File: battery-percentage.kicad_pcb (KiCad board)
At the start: 2 copper layers, 52.1 x 40.6 mm, 11 parts, among them J1 Conn_01x04_Pin, SW1 SW_Push, U1 WeMos_D1_mini, U2 LM7805_TO220

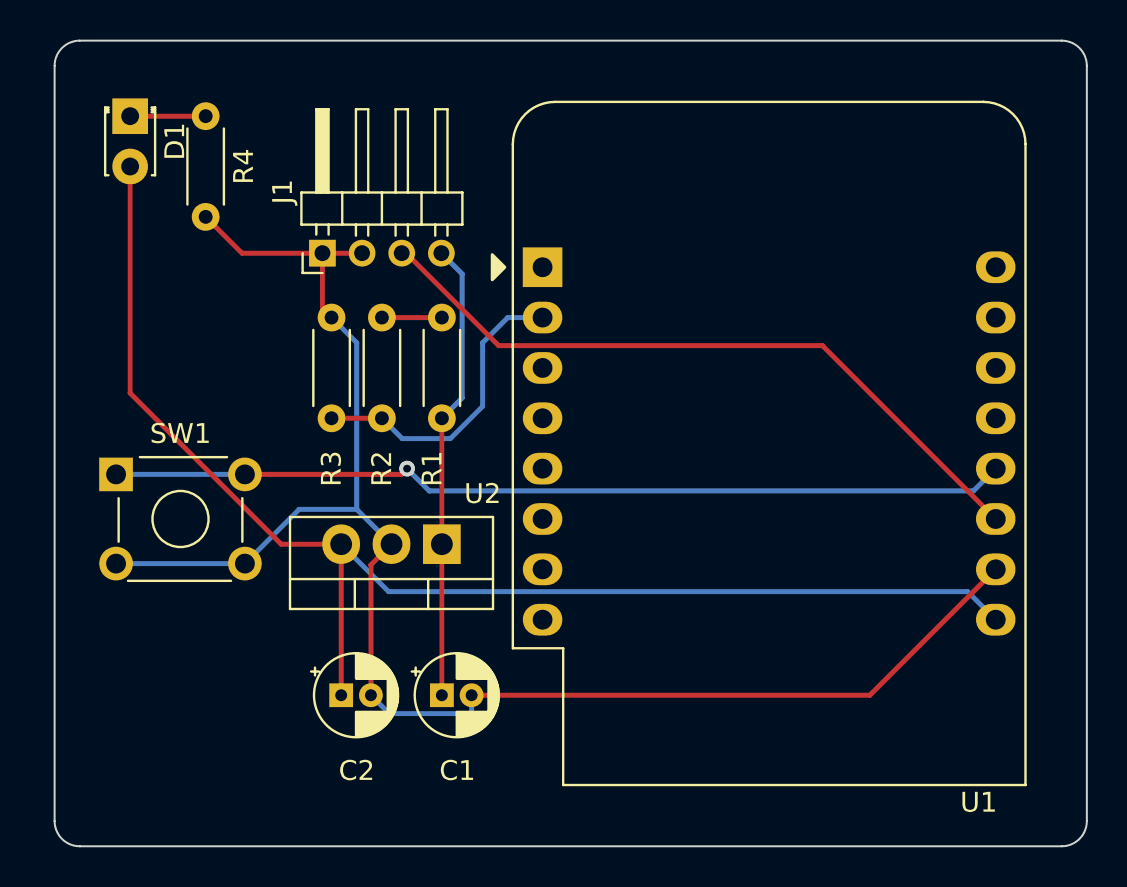
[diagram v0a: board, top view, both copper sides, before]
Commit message: Added TTl Interface to PCB
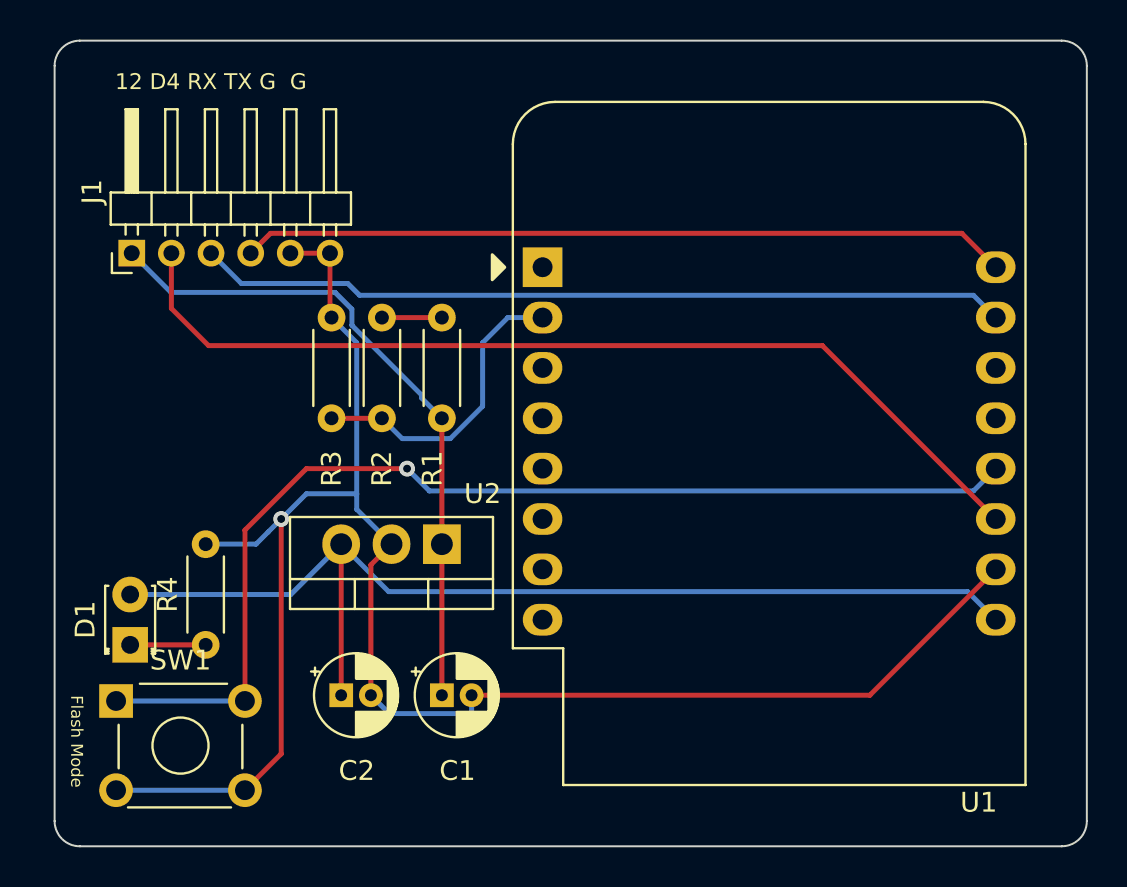
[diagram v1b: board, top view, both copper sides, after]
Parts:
- J1: value Conn_01x04_Pin -> Conn_01x06; footprint Connector_PinHeader_2.00mm:PinHeader_1x04_P2.00mm_Horizontal -> Connector_PinHeader_2.00mm:PinHeader_1x06_P2.00mm_Horizontal
- moved D1 26.7 mm to (64.8, 80.0), turned to 90 degrees
- moved R4 26.7 mm to (68.6, 80.0), turned to 90 degrees
- moved SW1 11.4 mm to (64.1, 82.8)
- moved J1 9.62 mm to (64.8, 60.2)
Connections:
- J1 pad 1: GND -> +12V
- J1 pad 2: GND -> /D4
- J1 pad 3: /D4 -> /RX
- J1 pad 4: +12V -> /TX
- U1 pad 15: unconnected-(U1-RX-Pad15) -> /RX
- U1 pad 16: unconnected-(U1-TX-Pad16) -> /TX
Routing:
- net /RX: track 0.00 -> 40.9 mm
- net /TX: track 0.00 -> 38.7 mm
- net +5V: track 67.4 -> 53.9 mm
- net /D4: track 35.5 -> 48.8 mm
- net +12V: track 23.2 -> 33.6 mm
- net /FLASH: track 45.4 -> 55.2 mm
- net GND: track 81.5 -> 91.0 mm, vias 0 -> 1
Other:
- board text added: "12 D4 RX TX G G"
- board text added: "Flash Mode"

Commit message: Updated PCB
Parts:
- added C3: 0.1uF, Capacitor_THT:CP_Radial_D4.0mm_P1.50mm, F.Cu at (74.9, 82.5)
- C1: value 0.33uF -> 0.2uF
- R1: value 120k -> 10k
- R3: value 10k -> 120k
- moved SW1 9.27 mm to (62.8, 73.7)
- moved D1 9.27 mm to (63.5, 70.8)
- moved R4 9.27 mm to (67.3, 70.8)
- moved C2 7.07 mm to (68.3, 82.5)
- turned C1 to 180 degrees
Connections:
- C1 pad 2: GND -> Net-(C1-Pad2)
- R1 pad 2: Net-(R1-Pad2) -> /A0
- R2 pad 1: Net-(R1-Pad2) -> /A0
- R2 pad 2: /A0 -> Net-(R2-Pad2)
- R3 pad 1: /A0 -> Net-(R2-Pad2)
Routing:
- net GND: track 91.0 -> 83.3 mm
- net /FLASH: track 55.2 -> 47.6 mm
- net +5V: track 53.9 -> 60.7 mm
- net Net-(C1-Pad2): track 0.00 -> 4.06 mm
- net Net-(R1-Pad2): track 3.03 -> 0.00 mm
- net /A0: track 15.5 -> 18.5 mm
